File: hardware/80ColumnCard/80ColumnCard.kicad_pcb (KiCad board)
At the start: 2 copper layers, 155.2 x 78.6 mm, 48 parts, among them J1 Apple II Expansion Bus, J2 VIDEO & LIGHT PEN, Q1 2N3904, U1 74LS86, U10 6116, U10N28 '32 - '256, U10N32 '512, U10W24 6116, U10W28 '32 - '256, U10W32 '512, U14 74LS157, U15 74LS157, U16 74LS157, U18 74LS273, U19 MC6845, U2 74LS02, U20 2732, U20W28 '64 - '512, U20W32 '010 - '080, U21 74LS166, U22 74LS175, U23 74LS161, U3 2758/'16/'32, U3W28 '64 - '512, U4 74LS04, U5 74LS245, U6 74LS00, U7 4013, U8 4013, U9 74LS139, X21 A11/WE, X6 CHAR INV, X7 SCREEN INV, Y1 17.430 MHZ

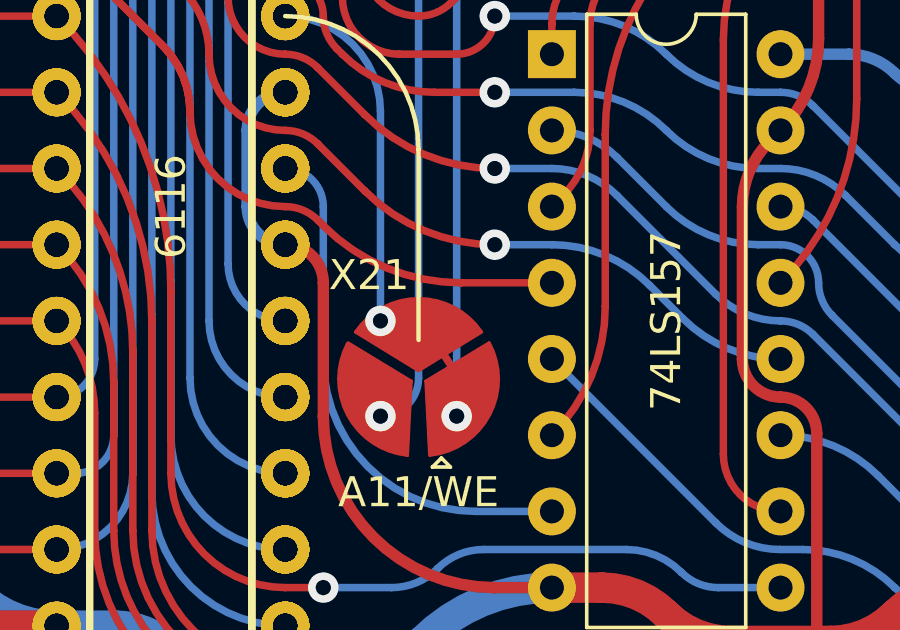
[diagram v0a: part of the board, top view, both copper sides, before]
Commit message: DEV->DEVICE_SELECT
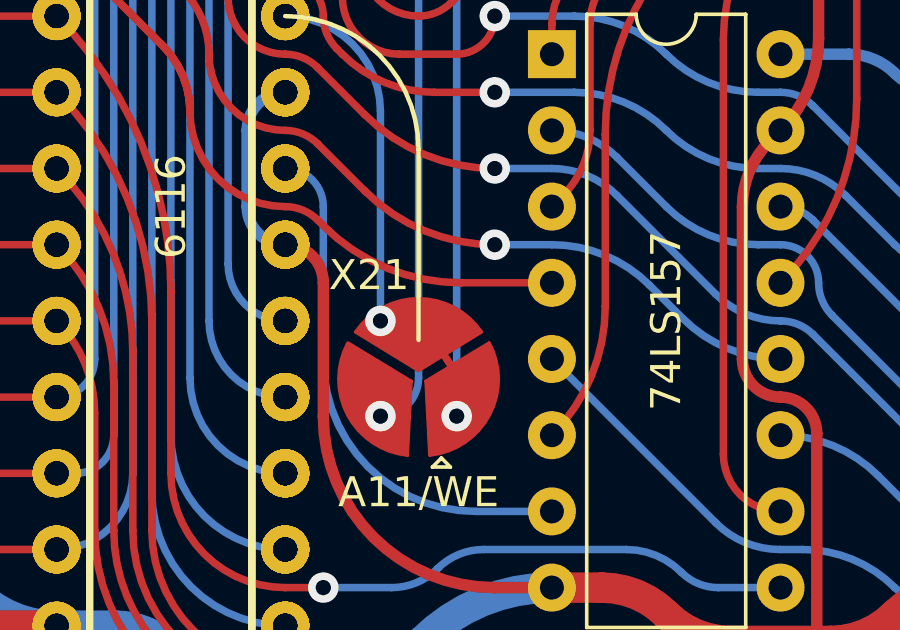
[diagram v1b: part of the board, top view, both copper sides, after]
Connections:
- net /DEV renamed /DEVICE_SELECT
- net /~{DEV} renamed /~{DEVICE_SELECT}
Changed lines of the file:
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@@
   (net 144 "/-12V")
   (net 145 "-5V")
-  (net 146 "/~{DEV}")
+  (net 146 "/~{DEVICE_SELECT}")
   (net 147 "+12V")
   (net 148 "Net-(U4-Pad12)")
   (net 149 "/HSYNC")
   (net 150 "/VSYNC")
-  (net 151 "/DEV")
+  (net 151 "/DEVICE_SELECT")
   (net 152 "/SRAM/RAM_R{slash}~{W}")
   (net 153 "/SRAM/RAMA5")
@@
             (gr_line (start 0.720183 -2.106487) (end -0.5715 0) (width 0.1))
     (gr_arc (start 0.720183 -2.106487) (mid 1.541357 -1.196944) (end 1.84148 -0.00887) (width 0.1))
-    (gr_arc (start 1.8415 0) (mid 1.548053 1.184689) (end 0.735952 2.095783) (width 0.1))
+    (gr_arc (start 1.8415 0) (mid 1.549086 1.182728) (end 0.739608 2.093276) (width 0.1))
       ))
     (pad "3" smd custom (at -0.3556 -0.8128 90) (size 0.0254 0.0254) (layers "F.Cu" "F.Mask")
@@
       (net 44 "/R{slash}~{W}") (pinfunction "R/~{W}") (pintype "input"))
     (pad "23" thru_hole oval (at 15.24 43.18 90) (size 1.6 1.6) (drill 0.8) (layers *.Cu *.Mask)
-      (net 151 "/DEV") (pinfunction "E") (pintype "input"))
+      (net 151 "/DEVICE_SELECT") (pinfunction "E") (pintype "input"))
     (pad "24" thru_hole oval (at 15.24 40.64 90) (size 1.6 1.6) (drill 0.8) (layers *.Cu *.Mask)
       (net 31 "/A0") (pinfunction "RS") (pintype "input"))
@@
       (net 18 "Net-(U1-Pad10)") (pintype "input"))
     (pad "11" thru_hole oval (at 7.62 7.62 90) (size 1.6 1.6) (drill 0.8) (layers *.Cu *.Mask)
-      (net 151 "/DEV") (pintype "output"))
+      (net 151 "/DEVICE_SELECT") (pintype "output"))
     (pad "12" thru_hole oval (at 7.62 5.08 90) (size 1.6 1.6) (drill 0.8) (layers *.Cu *.Mask)
-      (net 146 "/~{DEV}") (pintype "input"))
+      (net 146 "/~{DEVICE_SELECT}") (pintype "input"))
     (pad "13" thru_hole oval (at 7.62 2.54 90) (size 1.6 1.6) (drill 0.8) (layers *.Cu *.Mask)
       (net 5 "+5V") (pintype "input"))
@@
       (net 1 "GND") (pinfunction "R") (pintype "input"))
     (pad "11" thru_hole oval (at 7.62 7.62 90) (size 1.6 1.6) (drill 0.8) (layers *.Cu *.Mask)
-      (net 151 "/DEV") (pinfunction "C") (pintype "input"))
+      (net 151 "/DEVICE_SELECT") (pinfunction "C") (pintype "input"))
     (pad "12" thru_hole oval (at 7.62 5.08 90) (size 1.6 1.6) (drill 0.8) (layers *.Cu *.Mask)
       (net 59 "unconnected-(U7-Pad12)") (pinfunction "~{Q}") (pintype "output+no_connect"))
@@
       (net 62 "unconnected-(U8-Pad2)") (pinfunction "~{Q}") (pintype "output+no_connect"))
     (pad "3" thru_hole oval (at 0 5.08 90) (size 1.6 1.6) (drill 0.8) (layers *.Cu *.Mask)
-      (net 151 "/DEV") (pinfunction "C") (pintype "input"))
+      (net 151 "/DEVICE_SELECT") (pinfunction "C") (pintype "input"))
     (pad "4" thru_hole oval (at 0 7.62 90) (size 1.6 1.6) (drill 0.8) (layers *.Cu *.Mask)
       (net 1 "GND") (pinfunction "R") (pintype "input"))
@@
       (net 1 "GND") (pinfunction "R") (pintype "input"))
     (pad "11" thru_hole oval (at 7.62 7.62 90) (size 1.6 1.6) (drill 0.8) (layers *.Cu *.Mask)
-      (net 151 "/DEV") (pinfunction "C") (pintype "input"))
+      (net 151 "/DEVICE_SELECT") (pinfunction "C") (pintype "input"))
     (pad "12" thru_hole oval (at 7.62 5.08 90) (size 1.6 1.6) (drill 0.8) (layers *.Cu *.Mask)
       (net 63 "unconnected-(U8-Pad12)") (pinfunction "~{Q}") (pintype "output+no_connect"))
@@
       (net 134 "/PHI0") (pinfunction "PHI0") (pintype "passive"))
     (pad "41" connect roundrect locked (at -7.62 0) (size 1.27 7.366) (layers "B.Cu" "B.Mask") (roundrect_rratio 0.25)
-      (net 146 "/~{DEV}") (pinfunction "~{DEVICE_SELECT}") (pintype "passive"))
+      (net 146 "/~{DEVICE_SELECT}") (pinfunction "~{DEVICE_SELECT}") (pintype "passive"))
     (pad "42" connect roundrect locked (at -10.16 0) (size 1.27 7.366) (layers "B.Cu" "B.Mask") (roundrect_rratio 0.25)
       (net 39 "/D7") (pinfunction "D7") (pintype "passive"))

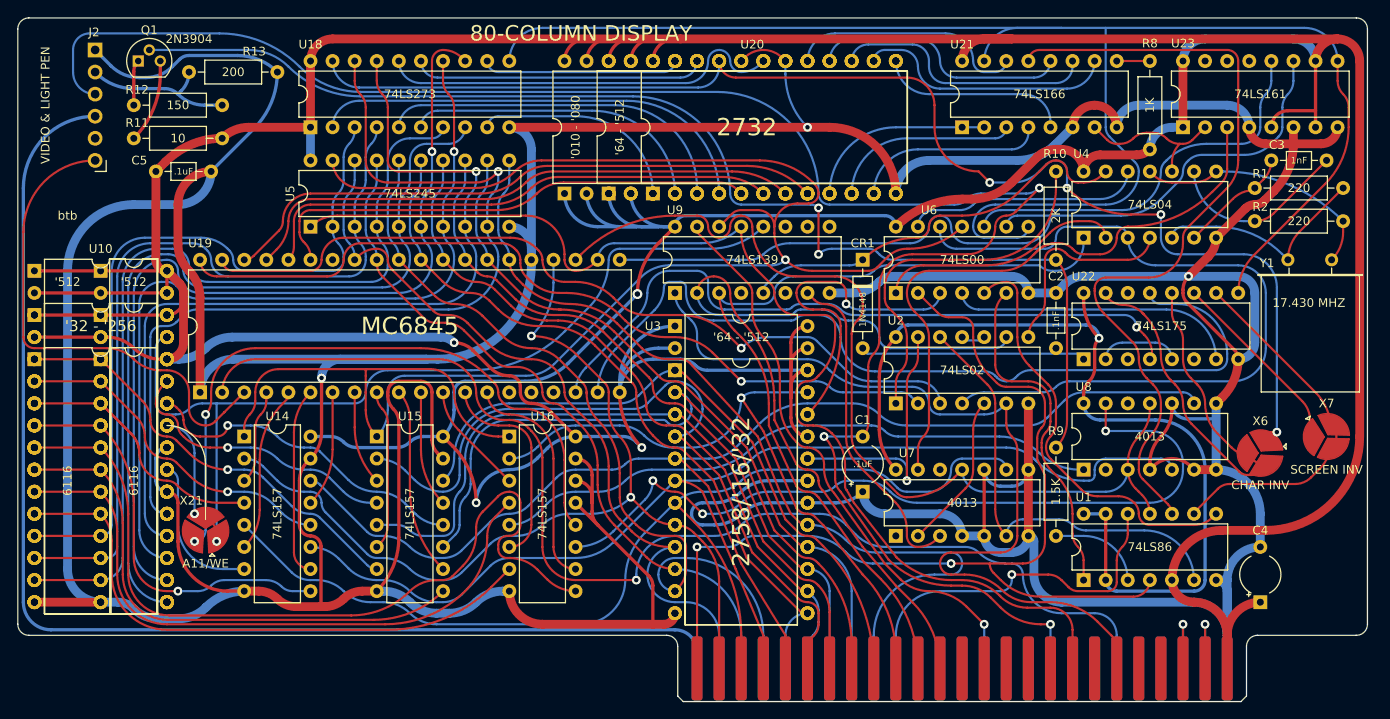
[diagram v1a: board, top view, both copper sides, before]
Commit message: connect CRTC A11 to SRAM multiplexer. add jumpers for selectable firmware
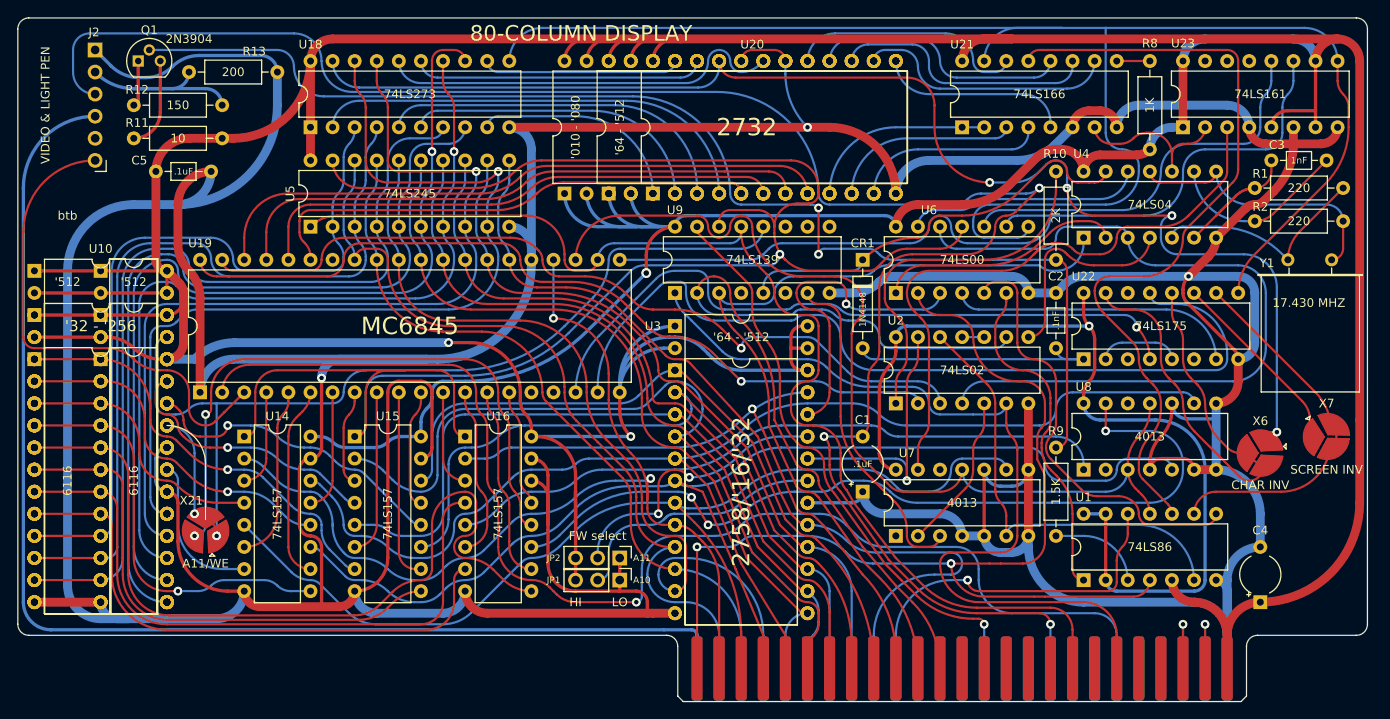
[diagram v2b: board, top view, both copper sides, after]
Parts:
- added JP1: A10, Connector_PinHeader_2.54mm:PinHeader_1x03_P2.54mm_Vertical, F.Cu at (162.6, 116.8)
- added JP2: A11, Connector_PinHeader_2.54mm:PinHeader_1x03_P2.54mm_Vertical, F.Cu at (162.6, 114.3)
- moved U16 5.08 mm to (144.8, 100.3)
- moved U15 2.54 mm to (132.1, 100.3)
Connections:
- U16 pad 13: GND -> /B11
- U19 pad 15: unconnected-(U19-Pad15) -> /B11
- U3 pad 19: GND -> Net-(U3-Pad19)
- U3 pad 21: +5V -> Net-(U3-Pad21)
- U3W28 pad 21: GND -> Net-(U3-Pad19)
- U3W28 pad 23: +5V -> Net-(U3-Pad21)
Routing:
- net Net-(U3-Pad21): track 0.00 -> 32.9 mm, vias 0 -> 2
- net Net-(U3-Pad19): track 0.00 -> 31.2 mm
- net /B11: track 0.00 -> 13.4 mm
- net +5V: track 834.8 -> 822.3 mm, vias 5 -> 4
- net /fA9: track 69.9 -> 76.8 mm
- net /SRAM/RAMA0: track 36.9 -> 30.1 mm
- net Net-(C3-Pad1): track 12.8 -> 19.0 mm
- net /RAM_~{A}/B: track 206.6 -> 212.6 mm
- net /~{RES}: track 136.8 -> 142.0 mm
- net /VIDEO: track 18.3 -> 23.3 mm
- net /A7: track 75.3 -> 79.9 mm
- net /fA10: track 93.0 -> 97.4 mm
- net /~{IO_SELECT}: track 115.6 -> 120.0 mm
- net /A0: track 111.4 -> 115.8 mm
- net /A5: track 81.1 -> 85.2 mm
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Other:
- board text added: "FW select"
- board text added: "HI"
- board text added: "LO"

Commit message: clean up, add jumpers for fw/char selection
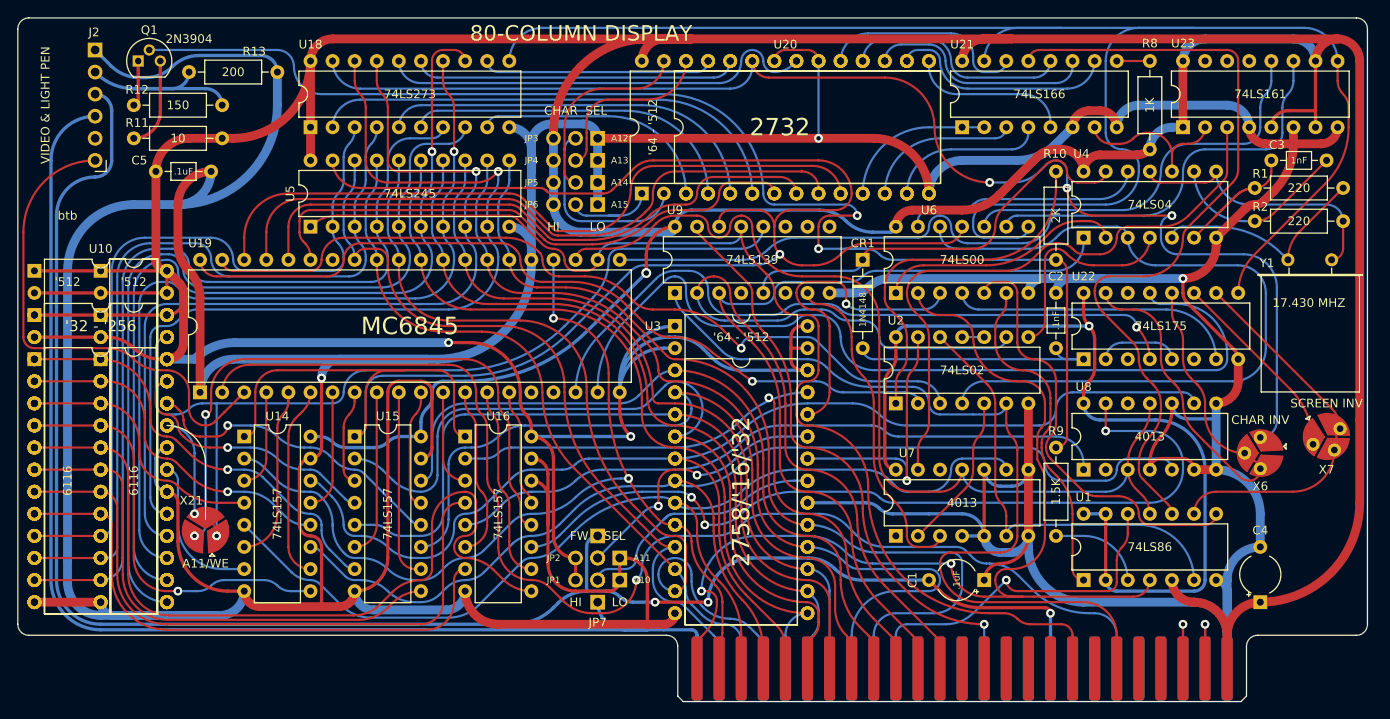
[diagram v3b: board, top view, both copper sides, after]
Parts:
- removed U20W32: '010 - '080, Package_DIP:DIP-32_W15.24mm
- added JP3: A12, Connector_PinHeader_2.54mm:PinHeader_1x03_P2.54mm_Vertical, F.Cu at (160.0, 66.0)
- added JP4: A13, Connector_PinHeader_2.54mm:PinHeader_1x03_P2.54mm_Vertical, F.Cu at (160.0, 68.6)
- added JP5: A14, Connector_PinHeader_2.54mm:PinHeader_1x03_P2.54mm_Vertical, F.Cu at (160.0, 71.1)
- added JP6: A15, Connector_PinHeader_2.54mm:PinHeader_1x03_P2.54mm_Vertical, F.Cu at (160.0, 73.7)
- added JP7: Jumper_2_Open, Connector_PinHeader_2.54mm:PinHeader_1x02_P2.54mm_Vertical, F.Cu at (160.0, 119.4)
- added JP8: Jumper_2_Open, Connector_PinHeader_2.54mm:PinHeader_1x02_P2.54mm_Vertical, F.Cu at (160.0, 111.8)
- moved C1 17.3 mm to (204.5, 116.8), turned to 180 degrees
- moved U20 3.81 mm to (170.2, 72.4)
- moved U20W28 3.81 mm to (165.1, 72.4)
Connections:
- net Net-(U3-Pad19) renamed /Firmware/A10
- net Net-(U3-Pad21) renamed /Firmware/A11
- U20 pad 24: +5V -> /Character ROM/ROMA9
- U20W28 pad 1: +5V -> /Character ROM/ROMA11
- U20W28 pad 2: +5V -> /Character ROM/ROMA8
- U20W28 pad 26: +5V -> /Character ROM/ROMA9
- U20W28 pad 27: +5V -> /Character ROM/ROMA10
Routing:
- net /Character ROM/ROMA8: track 0.00 -> 23.4 mm
- net /Character ROM/ROMA10: track 0.00 -> 22.5 mm
- net -5V: track 218.4 -> 196.7 mm
- net GND: track 815.3 -> 836.4 mm
- net /Character ROM/ROMA9: track 0.00 -> 20.3 mm
- net /D6: track 81.8 -> 101.0 mm
- net /Character ROM/ROMA11: track 0.00 -> 10.8 mm
- net Net-(Q1-Pad2): track 142.8 -> 152.0 mm
- net /RA0: track 72.5 -> 81.1 mm
- net Net-(U18-Pad11): track 190.7 -> 199.0 mm
- net /RA1: track 67.3 -> 75.5 mm
- net /RA2: track 61.6 -> 68.8 mm
- net /RA3: track 57.4 -> 64.5 mm
- net /RAM_~{A}/B: track 212.6 -> 218.8 mm
- net /A0: track 115.8 -> 109.9 mm
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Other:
- board text added: "CHAR SEL"
- board text added: "FW SEL"
- board text removed: "FW select"

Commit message: more cleanups
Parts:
- moved JP3 0.64 mm to (159.4, 66.0)
- moved JP4 0.64 mm to (159.4, 68.6)
- moved JP5 0.64 mm to (159.4, 71.1)
- moved JP6 0.64 mm to (159.4, 73.7)
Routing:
- net +5V: track 818.9 -> 825.0 mm
- net GND: track 836.4 -> 833.5 mm
- net Net-(U19-Pad18): track 80.3 -> 81.0 mm
- net /Character ROM/ROMA8: track 23.4 -> 24.0 mm
- net /Character ROM/ROMA11: track 10.8 -> 11.5 mm
- net /~{RES}: track 139.5 -> 140.0 mm

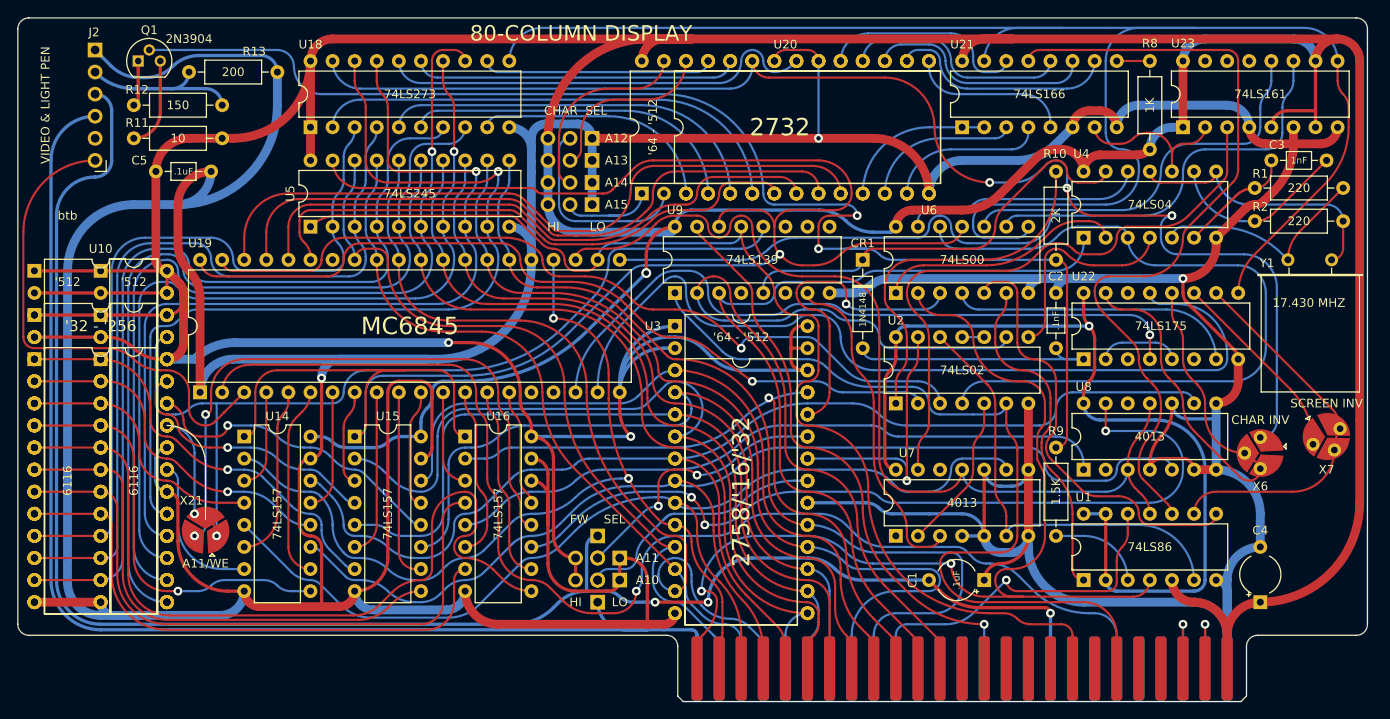
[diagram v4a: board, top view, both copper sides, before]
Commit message: use more common component sizes
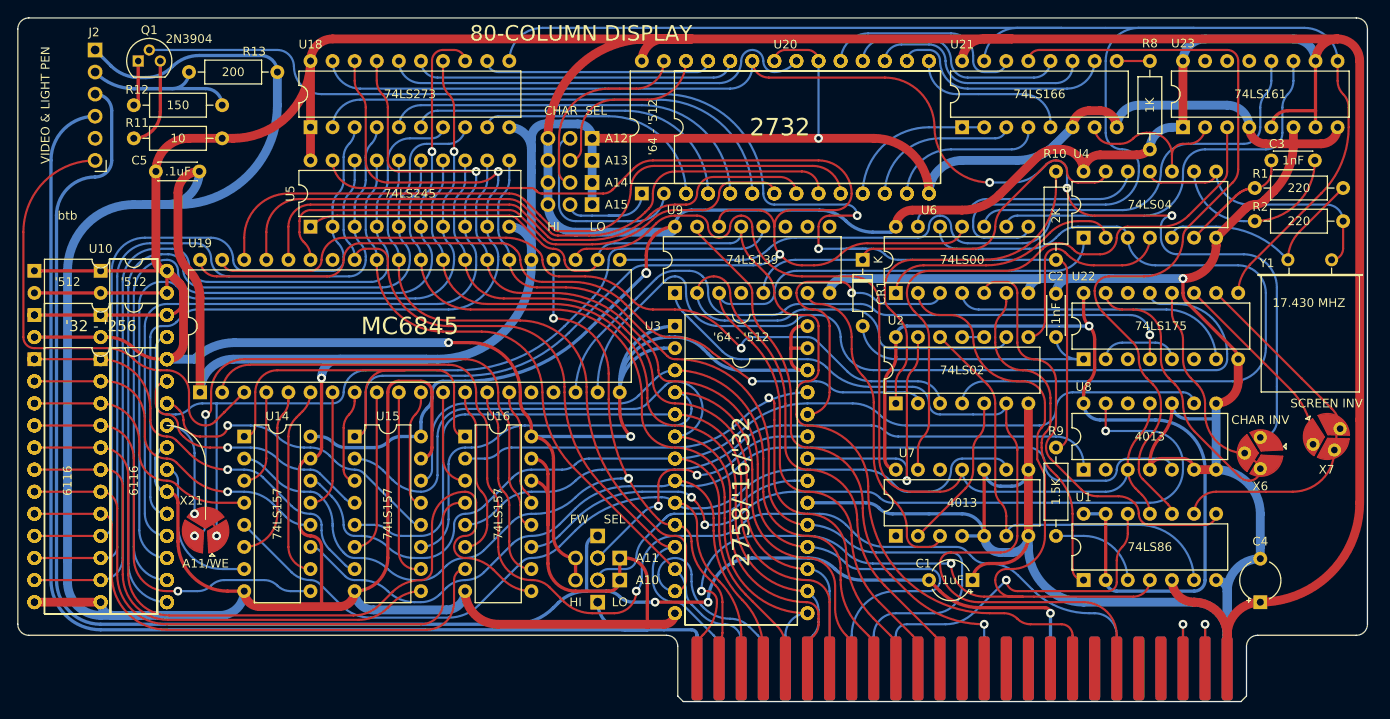
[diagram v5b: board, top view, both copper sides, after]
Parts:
- C1, C4: footprint MyPassives:CP_Radial_Tantal_D4.5mm_P6.35mm -> Capacitor_THT:CP_Radial_Tantal_D4.5mm_P5.00mm
- C2, C3, C5: footprint MyPassives:C_Axial_L2.6mm_D1.8mm_P6.35mm_Horizontal -> Capacitor_THT:C_Disc_D4.3mm_W1.9mm_P5.00mm
- CR1: footprint Diode_THT:D_DO-35_SOD27_P10.16mm_Horizontal -> Diode_THT:D_DO-35_SOD27_P7.62mm_Horizontal
- moved C1 1.35 mm to (203.1, 116.8)
- moved C2 1.27 mm to (212.7, 88.9)
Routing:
- net GND: track 833.5 -> 842.6 mm
- net Net-(C2-Pad1): track 29.9 -> 31.9 mm
- net /Firmware/A9: track 37.6 -> 36.2 mm
- net /DEVICE_SELECT: track 110.4 -> 111.3 mm

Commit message: fab doc for C1,C4
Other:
- board text added: "C1: only needed for light pen or 2708"
- board text added: "C4: optional"
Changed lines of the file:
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@@
+    (effects (font (size 1 1) (thickness 0.15)))
+  )
+  (gr_text "C1: only needed for light pen or 2708" (at 201.295 132.715) (layer "F.Fab")
+    (effects (font (size 1 1) (thickness 0.15)))
+  )
+  (gr_text "C4: optional" (at 254.635 115.57) (layer "F.Fab")
     (effects (font (size 1 1) (thickness 0.15)))
   )
